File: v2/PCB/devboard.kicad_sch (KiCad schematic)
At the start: 32 parts, among them J1 USB_C_Receptacle_USB2.0_14P, J2 Conn_01x20, J3 Conn_01x20, J4 Conn_01x03, SW1 SW_Push, U1 RP2040, U2 MCP1700x-330xxTT, U3 W25Q16JVUXIQ TR, Y1 Crystal_GND24

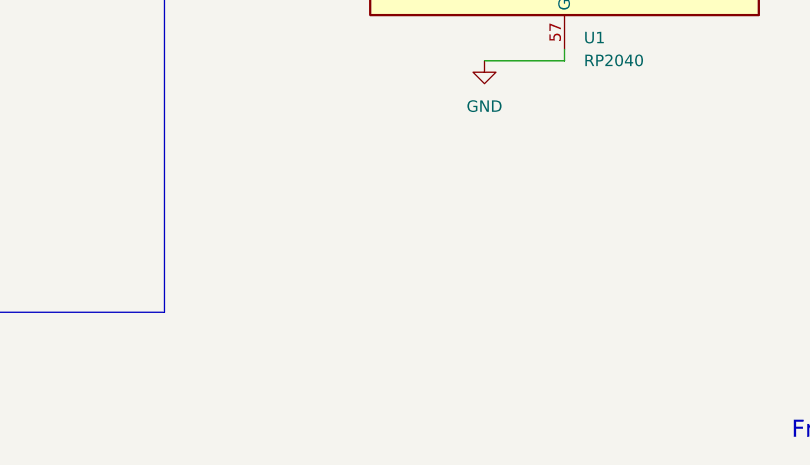
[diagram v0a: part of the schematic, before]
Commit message: added v1 folder
added leds to the v1 board and created a v2 folder
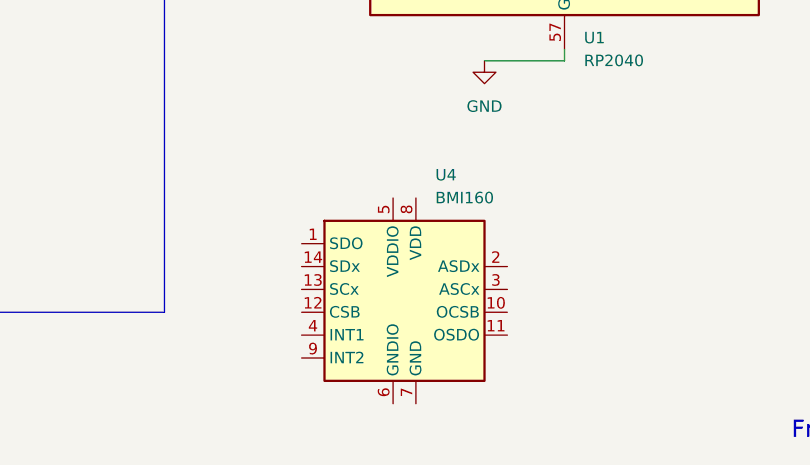
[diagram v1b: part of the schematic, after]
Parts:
- added U4: BMI160, Package_LGA:Bosch_LGA-14_3x2.5mm_P0.5mm, symbol Sensor_Motion:BMI160
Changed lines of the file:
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@@
+	)
+	(symbol
+		(lib_id "Sensor_Motion:BMI160")
+		(at 144.78 173.99 0)
+		(unit 1)
+		(body_style 1)
+		(exclude_from_sim no)
+		(in_bom yes)
+		(on_board yes)
+		(in_pos_files yes)
+		(dnp no)
+		(fields_autoplaced yes)
+		(property "Reference" "U4"
+			(at 146.9233 161.29 0)
+			(show_name no)
+			(do_not_autoplace no)
+			(effects
+				(font
+					(size 1.27 1.27)
+				)
+				(justify left)
+			)
+		)
+		(property "Value" "BMI160"
+			(at 146.9233 163.83 0)
+			(show_name no)
+			(do_not_autoplace no)
+			(effects
+				(font
+					(size 1.27 1.27)
+				)
+				(justify left)
+			)
+		)
+		(property "Footprint" "Package_LGA:Bosch_LGA-14_3x2.5mm_P0.5mm"
+			(at 144.78 173.99 0)
+			(hide yes)
+			(show_name no)
+			(do_not_autoplace no)
+			(effects
+				(font
+					(size 1.27 1.27)
+				)
+			)
+		)
+		(property "Datasheet" "https://www.bosch-sensortec.com/media/boschsensortec/downloads/datasheets/bst-bmi160-ds000.pdf"
+			(at 127 152.4 0)
+			(hide yes)
+			(show_name no)
+			(do_not_autoplace no)
+			(effects
+				(font
+					(size 1.27 1.27)
+				)
+			)
+		)
+		(property "Description" "Small, low power inertial measurement unit, LGA-14"
+			(at 144.78 173.99 0)
+			(hide yes)
+			(show_name no)
+			(do_not_autoplace no)
+			(effects
+				(font
+					(size 1.27 1.27)
+				)
+			)
+		)
+		(pin "3"
+		)
+		(pin "5"
+		)
+		(pin "1"
+		)
+		(pin "6"
+		)
+		(pin "12"
+		)
+		(pin "2"
+		)
+		(pin "7"
+		)
+		(pin "14"
+		)
+		(pin "13"
+		)
+		(pin "11"
+		)
+		(pin "4"
+		)
+		(pin "8"
+		)
+		(pin "9"
+		)
+		(pin "10"
+		)
+		(instances
+			(project "devboard"
+				(path "/dee596ae-7713-49e5-a777-8ba88ca83085"
+					(reference "U4")
+					(unit 1)
+				)
+			)
+		)
 	)
 	(symbol
